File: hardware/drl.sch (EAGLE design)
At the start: 17 parts, among them IC1 TINY13-20SU, IC3 REG1117, Q1 IRF3205Z, Q2 IRF3205Z, T1 BC817-40, X1 CON1, X2 CON2

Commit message: Change in schematic and board.
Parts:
- added C4: 47u, rcl:CPOL-EUE2,5-6E
- added D1: (no value), semicon-smd-ipc:D-SOD-80
- added R5: 10k, rcl:R-EU_R0805
- C3: value 22u -> 100u
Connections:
- new net VCC12: C1.1, C4.+, D1.C, IC3.VIN, R4.2
- net +12: now also D1.A; no longer C1.1, IC3.VIN, R4.2
- net GND: now also C4.-
- net N$7: now also R5.2
- net VCC: now also R5.1
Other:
- moved on the sheet: C1, C2, C3, IC3, X1-1, X1-2, X2-1, X2-2
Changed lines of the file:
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@@
 <part name="C1" library="resistor" deviceset="C-EU" device="C0805K" value="100n"/>
 <part name="C2" library="resistor" deviceset="C-EU" device="C0805K" value="100n"/>
-<part name="C3" library="rcl" deviceset="CPOL-EU" device="E2,5-6E" value="22u"/>
+<part name="C3" library="rcl" deviceset="CPOL-EU" device="E2,5-6E" value="100u"/>
 <part name="IC3" library="burr-brown" deviceset="REG1117" device=""/>
 <part name="GND5" library="supply1" deviceset="GND" device=""/>
@@
 <part name="R1" library="rcl" deviceset="R-EU_" device="0204/7" value="100"/>
 <part name="R2" library="rcl" deviceset="R-EU_" device="0204/7" value="1k"/>
+<part name="C4" library="rcl" deviceset="CPOL-EU" device="E2,5-6E" value="47u"/>
+<part name="D1" library="semicon-smd-ipc" deviceset="D-" device="SOD-80"/>
+<part name="R5" library="rcl" deviceset="R-EU_" device="R0805" value="10k"/>
 </parts>
 <sheets>
@@
 <instance part="JP1" gate="G$1" x="76.2" y="71.12"/>
 <instance part="GND3" gate="1" x="78.74" y="45.72"/>
-<instance part="GND4" gate="1" x="60.96" y="63.5"/>
-<instance part="C1" gate="G$1" x="15.24" y="71.12"/>
-<instance part="C2" gate="G$1" x="45.72" y="71.12"/>
-<instance part="C3" gate="G$1" x="53.34" y="71.12"/>
-<instance part="IC3" gate="G$1" x="30.48" y="76.2"/>
-<instance part="GND5" gate="1" x="30.48" y="58.42"/>
+<instance part="GND4" gate="1" x="63.5" y="63.5"/>
+<instance part="C1" gate="G$1" x="20.32" y="71.12"/>
+<instance part="C2" gate="G$1" x="48.26" y="71.12"/>
+<instance part="C3" gate="G$1" x="55.88" y="71.12"/>
+<instance part="IC3" gate="G$1" x="35.56" y="76.2"/>
+<instance part="GND5" gate="1" x="35.56" y="58.42"/>
 <instance part="R6" gate="G$1" x="60.96" y="20.32" rot="R180"/>
 <instance part="R7" gate="G$1" x="76.2" y="20.32" rot="R180"/>
 <instance part="GND6" gate="1" x="83.82" y="15.24"/>
-<instance part="X1" gate="-1" x="-5.08" y="68.58"/>
-<instance part="X1" gate="-2" x="-5.08" y="63.5"/>
-<instance part="X2" gate="-1" x="-5.08" y="53.34"/>
-<instance part="X2" gate="-2" x="-5.08" y="48.26"/>
+<instance part="X1" gate="-1" x="-2.54" y="53.34"/>
+<instance part="X1" gate="-2" x="-2.54" y="48.26"/>
+<instance part="X2" gate="-1" x="-2.54" y="38.1"/>
+<instance part="X2" gate="-2" x="-2.54" y="33.02"/>
 <instance part="R1" gate="G$1" x="109.22" y="35.56"/>
 <instance part="R2" gate="G$1" x="81.28" y="35.56"/>
+<instance part="C4" gate="G$1" x="12.7" y="71.12"/>
+<instance part="D1" gate="G$1" x="10.16" y="76.2"/>
+<instance part="R5" gate="G$1" x="81.28" y="27.94" rot="R180"/>
 </instances>
 <busses>
@@
 <segment>
 <pinref part="JP1" gate="G$1" pin="6"/>
-<wire x1="71.12" y1="68.58" x2="60.96" y2="68.58" width="0.1524" layer="91"/>
-<wire x1="60.96" y1="68.58" x2="60.96" y2="66.04" width="0.1524" layer="91"/>
+<wire x1="71.12" y1="68.58" x2="63.5" y2="68.58" width="0.1524" layer="91"/>
+<wire x1="63.5" y1="68.58" x2="63.5" y2="66.04" width="0.1524" layer="91"/>
 <pinref part="GND4" gate="1" pin="GND"/>
 </segment>
 <segment>
 <pinref part="IC3" gate="G$1" pin="GND"/>
-<wire x1="30.48" y1="63.5" x2="30.48" y2="60.96" width="0.1524" layer="91"/>
-<wire x1="30.48" y1="60.96" x2="15.24" y2="60.96" width="0.1524" layer="91"/>
+<wire x1="35.56" y1="63.5" x2="35.56" y2="60.96" width="0.1524" layer="91"/>
+<wire x1="35.56" y1="60.96" x2="20.32" y2="60.96" width="0.1524" layer="91"/>
 <pinref part="C1" gate="G$1" pin="2"/>
-<wire x1="15.24" y1="60.96" x2="15.24" y2="66.04" width="0.1524" layer="91"/>
+<wire x1="20.32" y1="60.96" x2="20.32" y2="66.04" width="0.1524" layer="91"/>
 <pinref part="C2" gate="G$1" pin="2"/>
-<wire x1="45.72" y1="66.04" x2="45.72" y2="60.96" width="0.1524" layer="91"/>
-<wire x1="45.72" y1="60.96" x2="30.48" y2="60.96" width="0.1524" layer="91"/>
+<wire x1="48.26" y1="66.04" x2="48.26" y2="60.96" width="0.1524" layer="91"/>
+<wire x1="48.26" y1="60.96" x2="35.56" y2="60.96" width="0.1524" layer="91"/>
 <pinref part="C3" gate="G$1" pin="-"/>
-<wire x1="53.34" y1="66.04" x2="53.34" y2="60.96" width="0.1524" layer="91"/>
-<wire x1="53.34" y1="60.96" x2="45.72" y2="60.96" width="0.1524" layer="91"/>
+<wire x1="55.88" y1="66.04" x2="55.88" y2="60.96" width="0.1524" layer="91"/>
+<wire x1="55.88" y1="60.96" x2="48.26" y2="60.96" width="0.1524" layer="91"/>
 <pinref part="GND5" gate="1" pin="GND"/>
-<junction x="30.48" y="60.96"/>
-<junction x="45.72" y="60.96"/>
+<junction x="35.56" y="60.96"/>
+<junction x="48.26" y="60.96"/>
+<pinref part="C4" gate="G$1" pin="-"/>
+<wire x1="20.32" y1="60.96" x2="12.7" y2="60.96" width="0.1524" layer="91"/>
+<wire x1="12.7" y1="60.96" x2="12.7" y2="66.04" width="0.1524" layer="91"/>
+<junction x="20.32" y="60.96"/>
 </segment>
 <segment>
@@
 <segment>
 <pinref part="X1" gate="-2" pin="KL"/>
-<wire x1="0" y1="63.5" x2="5.08" y2="63.5" width="0.1524" layer="91"/>
-<label x="2.54" y="66.04" size="1.778" layer="95"/>
+<wire x1="2.54" y1="48.26" x2="7.62" y2="48.26" width="0.1524" layer="91"/>
+<label x="2.54" y="50.8" size="1.778" layer="95"/>
 </segment>
 </net>
@@
 <segment>
 <pinref part="X1" gate="-1" pin="KL"/>
-<wire x1="0" y1="68.58" x2="5.08" y2="68.58" width="0.1524" layer="91"/>
-<label x="2.54" y="71.12" size="1.778" layer="95"/>
+<wire x1="2.54" y1="53.34" x2="7.62" y2="53.34" width="0.1524" layer="91"/>
+<label x="2.54" y="55.88" size="1.778" layer="95"/>
 </segment>
 </net>
@@
 <junction x="73.66" y="35.56"/>
 <pinref part="R2" gate="G$1" pin="1"/>
+<pinref part="R5" gate="G$1" pin="2"/>
+<wire x1="73.66" y1="35.56" x2="73.66" y2="27.94" width="0.1524" layer="91"/>
+<wire x1="73.66" y1="27.94" x2="76.2" y2="27.94" width="0.1524" layer="91"/>
 </segment>
 </net>
@@
 <net name="+12" class="0">
 <segment>
-<pinref part="R4" gate="G$1" pin="2"/>
-<wire x1="93.98" y1="58.42" x2="93.98" y2="81.28" width="0.1524" layer="91"/>
-<label x="93.98" y="81.28" size="1.778" layer="95"/>
-</segment>
-<segment>
-<wire x1="15.24" y1="73.66" x2="15.24" y2="76.2" width="0.1524" layer="91"/>
-<pinref part="C1" gate="G$1" pin="1"/>
-<pinref part="IC3" gate="G$1" pin="VIN"/>
-<wire x1="15.24" y1="76.2" x2="15.24" y2="83.82" width="0.1524" layer="91"/>
-<wire x1="17.78" y1="76.2" x2="15.24" y2="76.2" width="0.1524" layer="91"/>
-<junction x="15.24" y="76.2"/>
-<label x="15.24" y="83.82" size="1.778" layer="95"/>
-</segment>
-<segment>
 <pinref part="X2" gate="-2" pin="KL"/>
-<wire x1="0" y1="48.26" x2="5.08" y2="48.26" width="0.1524" layer="91"/>
-<label x="2.54" y="50.8" size="1.778" layer="95"/>
+<wire x1="2.54" y1="33.02" x2="7.62" y2="33.02" width="0.1524" layer="91"/>
+<label x="2.54" y="35.56" size="1.778" layer="95"/>
+</segment>
+<segment>
+<pinref part="D1" gate="G$1" pin="A"/>
+<wire x1="7.62" y1="76.2" x2="2.54" y2="76.2" width="0.1524" layer="91"/>
+<label x="0" y="78.74" size="1.778" layer="95"/>
 </segment>
 </net>
@@
 <wire x1="66.04" y1="73.66" x2="66.04" y2="76.2" width="0.1524" layer="91"/>
 <pinref part="C2" gate="G$1" pin="1"/>
-<wire x1="45.72" y1="73.66" x2="45.72" y2="76.2" width="0.1524" layer="91"/>
+<wire x1="48.26" y1="73.66" x2="48.26" y2="76.2" width="0.1524" layer="91"/>
 <pinref part="IC3" gate="G$1" pin="VOUT"/>
-<wire x1="45.72" y1="76.2" x2="43.18" y2="76.2" width="0.1524" layer="91"/>
 <pinref part="C3" gate="G$1" pin="+"/>
-<wire x1="53.34" y1="73.66" x2="53.34" y2="76.2" width="0.1524" layer="91"/>
-<wire x1="53.34" y1="76.2" x2="45.72" y2="76.2" width="0.1524" layer="91"/>
-<junction x="45.72" y="76.2"/>
-<wire x1="66.04" y1="76.2" x2="53.34" y2="76.2" width="0.1524" layer="91"/>
-<junction x="53.34" y="76.2"/>
+<wire x1="55.88" y1="73.66" x2="55.88" y2="76.2" width="0.1524" layer="91"/>
+<wire x1="55.88" y1="76.2" x2="48.26" y2="76.2" width="0.1524" layer="91"/>
+<junction x="48.26" y="76.2"/>
+<wire x1="66.04" y1="76.2" x2="55.88" y2="76.2" width="0.1524" layer="91"/>
+<junction x="55.88" y="76.2"/>
 <junction x="66.04" y="73.66"/>
+</segment>
+<segment>
+<pinref part="R5" gate="G$1" pin="1"/>
+<wire x1="86.36" y1="27.94" x2="88.9" y2="27.94" width="0.1524" layer="91"/>
+<label x="86.36" y="27.94" size="1.778" layer="95"/>
 </segment>
 </net>
@@
 <segment>
 <pinref part="X2" gate="-1" pin="KL"/>
-<wire x1="0" y1="53.34" x2="5.08" y2="53.34" width="0.1524" layer="91"/>
-<label x="2.54" y="55.88" size="1.778" layer="95"/>
-</segment>
-</net>
+<wire x1="2.54" y1="38.1" x2="7.62" y2="38.1" width="0.1524" layer="91"/>
+<label x="2.54" y="40.64" size="1.778" layer="95"/>
+</segment>
+</net>
+<net name="VCC12" class="0">
+<segment>
+<wire x1="20.32" y1="73.66" x2="20.32" y2="76.2" width="0.1524" layer="91"/>
+<pinref part="C1" gate="G$1" pin="1"/>
+<pinref part="IC3" gate="G$1" pin="VIN"/>
+<wire x1="22.86" y1="76.2" x2="20.32" y2="76.2" width="0.1524" layer="91"/>
+<junction x="20.32" y="76.2"/>
+<pinref part="C4" gate="G$1" pin="+"/>
+<wire x1="20.32" y1="76.2" x2="12.7" y2="76.2" width="0.1524" layer="91"/>
+<wire x1="12.7" y1="76.2" x2="12.7" y2="73.66" width="0.1524" layer="91"/>
+<pinref part="D1" gate="G$1" pin="C"/>
+<junction x="12.7" y="76.2"/>
+<pinref part="R4" gate="G$1" pin="2"/>
+<wire x1="93.98" y1="58.42" x2="93.98" y2="83.82" width="0.1524" layer="91"/>
+<wire x1="93.98" y1="83.82" x2="20.32" y2="83.82" width="0.1524" layer="91"/>
+<wire x1="20.32" y1="83.82" x2="20.32" y2="76.2" width="0.1524" layer="91"/>
+</segment>
+</net>

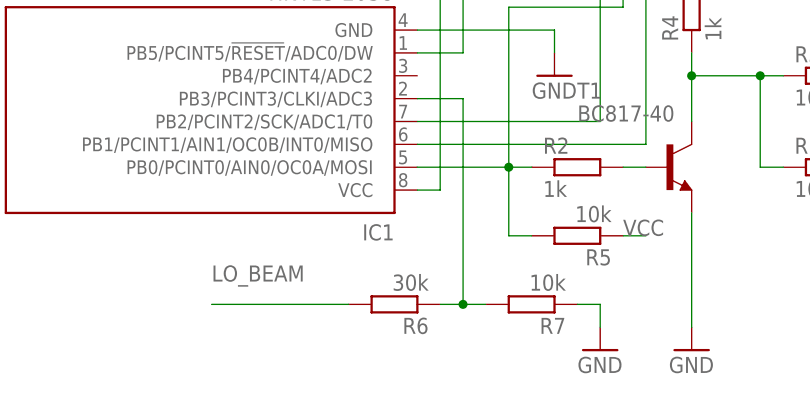
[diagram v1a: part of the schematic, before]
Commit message: Resistor value was edited
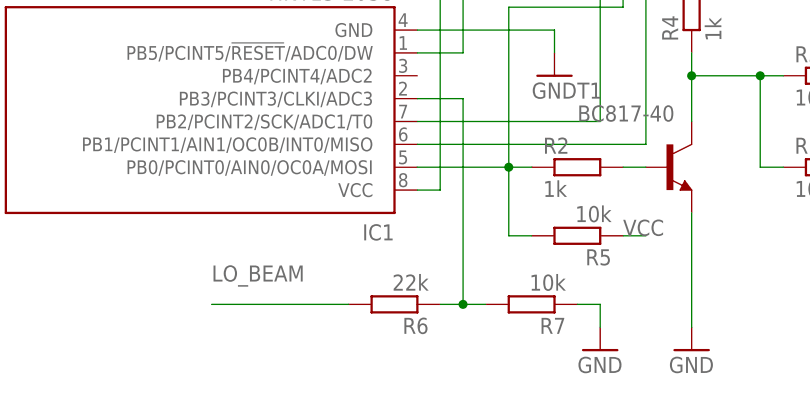
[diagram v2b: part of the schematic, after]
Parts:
- R6: value 30k -> 22k
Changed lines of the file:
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@@
 <part name="IC3" library="burr-brown" deviceset="REG1117" device=""/>
 <part name="GND5" library="supply1" deviceset="GND" device=""/>
-<part name="R6" library="rcl" deviceset="R-EU_" device="R0805" value="30k"/>
+<part name="R6" library="rcl" deviceset="R-EU_" device="R0805" value="22k"/>
 <part name="R7" library="rcl" deviceset="R-EU_" device="R0805" value="10k"/>
 <part name="GND6" library="supply1" deviceset="GND" device=""/>

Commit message: Second version of hardware (schematic and pcb)
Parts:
- removed IC3: REG1117, burr-brown:REG1117
- added C5, C6: 100n, resistor:C-EUC0805K
- added D2: (no value), semicon-smd-ipc:D-SOD-80
- added IC2: (no value), my_stuff:UA78L05SOIC
- added R10, R8: 10k, rcl:R-EU_R0805
- added R9: 22k, rcl:R-EU_R0805
- added S1: (no value), switch-omron:10-XX
- C3: value 100u -> 10u; device rcl:CPOL-EUE2,5-6E -> rcl:CPOL-EUSMCD
- C4: value 47u -> 10u; device rcl:CPOL-EUE2,5-6E -> rcl:CPOL-EUSMCD
- Q1, Q2: value IRF3205Z -> IRF3205; device my_stuff:IRF3205Z -> my_stuff:IRF3205
- R1: device rcl:R-EU_0204/7 -> rcl:R-EU_R0805
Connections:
- removed net LO_BEAM: R6.2, X2-1.KL
- removed net N$5: IC1.PB1/PCINT1/AIN1/OC0B/INT0/MISO, JP1.1
- new net N$11: IC1.PB0/PCINT0/AIN0/OC0A/MOSI, JP1.4, R2.1, R5.1
- new net N$12: IC1.PB1/PCINT1/AIN1/OC0B/INT0/MISO, JP1.1, S1.P1
- new net N$14: C6.1, IC1.PB4/PCINT4/ADC2, R8.1, R9.2
- new net N$2: D2.C, R6.2
- net GND: now also C5.2, C6.2, IC2.GND, R8.2, S1.S, S1.S1, X1-1.KL; no longer IC3.GND, X1-2.KL
- net HI_BEAM: now also X1-2.KL; no longer X1-1.KL
- net N$10: now also R10.2
- net N$7: now also D2.A, X2-1.KL; no longer IC1.PB0/PCINT0/AIN0/OC0A/MOSI, JP1.4, R2.1, R5.2
- net N$9: now also C5.1
- net VCC: now also C4.+, IC2.OUT, R10.1, R5.2; no longer C3.+, IC3.VOUT, R5.1
- net VCC12: now also C3.+, IC2.IN, R9.1; no longer C4.+, IC3.VIN
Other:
- moved on the sheet: C1, C3, C4, X1-1, X1-2, X2-1, X2-2

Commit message: Small editions in schematic and board design.
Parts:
- D1, D2: value (none) -> LL4148
- IC2: value (none) -> 5V
- S1: value (none) -> MODE
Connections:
- net N$7 renamed LOW_BEAM_IN
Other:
- moved on the sheet: C6, IC1, Q1, Q2, R1, R2, R3, R4, R8, R9, T1
